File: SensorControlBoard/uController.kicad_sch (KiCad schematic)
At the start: 37 parts, among them J10 Conn_01x05_Pin, J11 USB_C_Receptacle_USB2.0, J2 Conn_01x02_Pin, J3 Conn_01x10_Pin, J4 Conn_01x10_Pin, J5 Conn_01x10_Pin, J6 Conn_01x02_Pin, J7 Conn_01x02_Pin, J8 Conn_01x02_Pin, SW1 SW_SPDT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

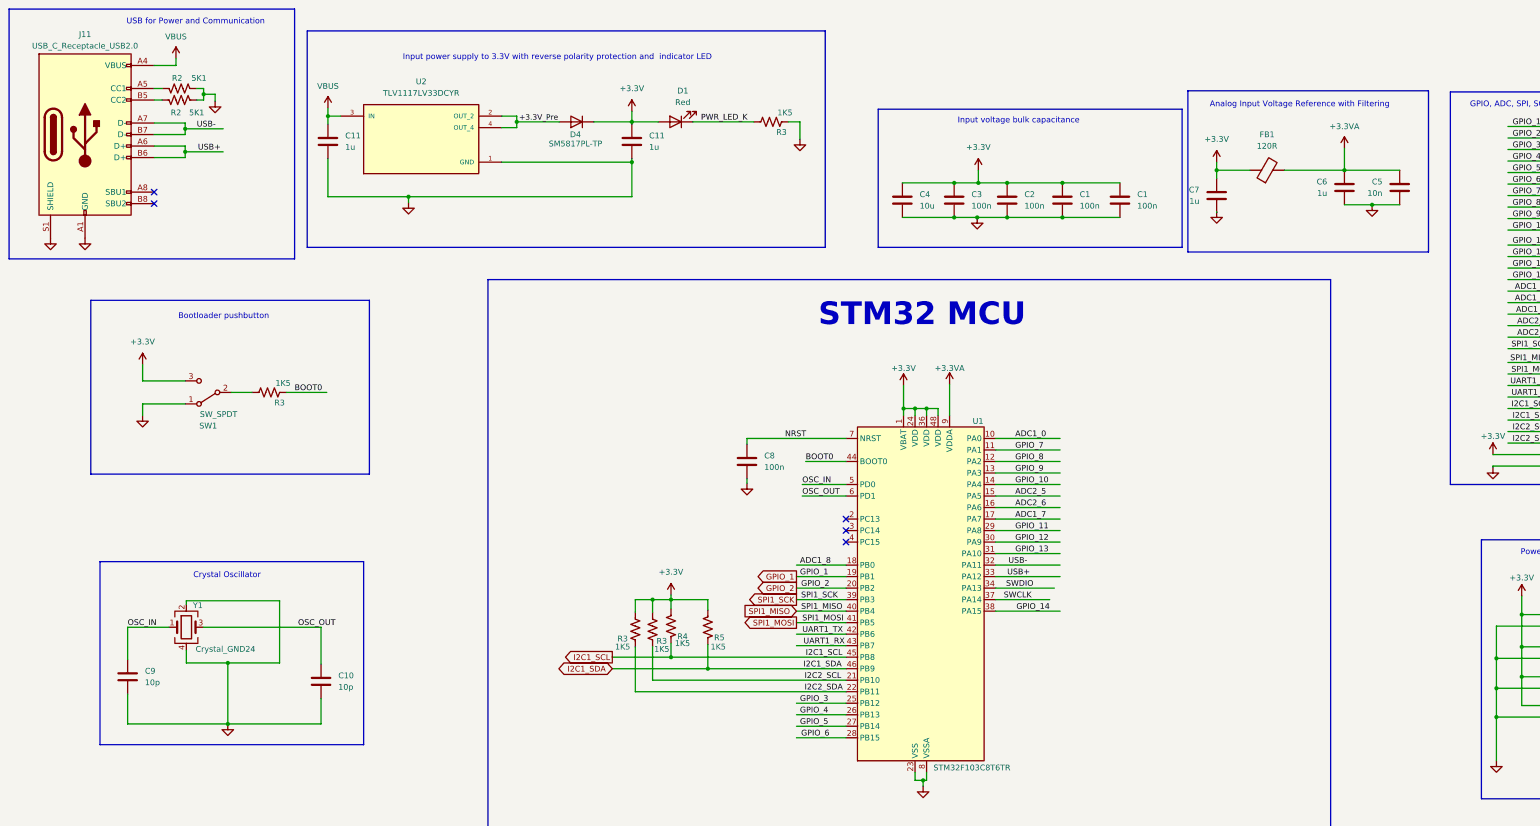
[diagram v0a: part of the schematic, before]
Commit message: Implemented ICM-42670-P 6 axis gyroscope/accelerometer
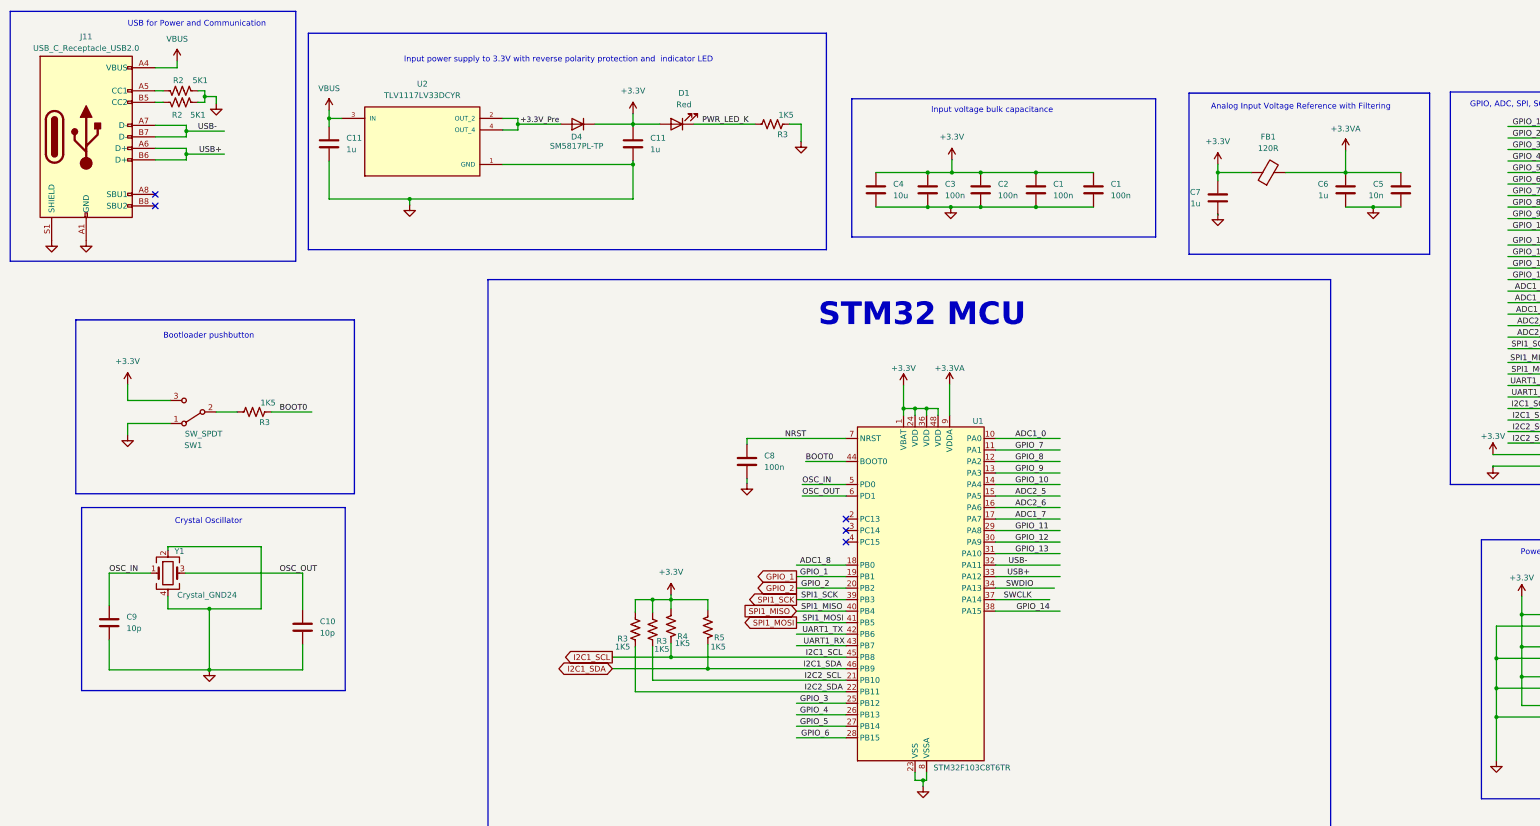
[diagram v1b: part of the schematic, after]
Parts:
- C1, C10, C11, C2, C3, C4, C5, C6, C7, C8, C9, D1, FB1, R2, R3, R4, R5, SW1, Y1: footprint (none) -> Resistor_SMD:R_0805_2012Metric
- J10: footprint (none) -> Connector_PinHeader_1.00mm:PinHeader_1x05_P1.00mm_Vertical
- J3: footprint (none) -> Connector_PinHeader_1.00mm:PinHeader_1x10_P1.00mm_Vertical
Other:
- moved on the sheet: C1, C10, C11, C2, C3, C4, C5, C6, C7, C9, D1, D4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

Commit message: Added more schematic documentation to prepare for hardware layout
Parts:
- Y1: value Crystal_GND24 -> 16MHz OSC; PN (none) -> X322516MMB4SI
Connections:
- net +3.3V: no longer J5.9 (Pin_9)
- net BOOT0: now also J5.10 (Pin_10)
- net GND: no longer J5.10 (Pin_10)
- net NRST: now also J5.9 (Pin_9)
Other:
- note added: "1: CS for TMAG5170 2: ALERT Pin for TMAG5170 3: ENABLE for LP5018 4: INT Pin for TMAG5273 5: CS for Micro-sd card 6: INT pin for OPT3002DNPR 7: INT1 for ICM-42670-P accel/gyro 8: INT2 for ICM-42670-P accel/gyro"
- note added: "1: SCL/SDA for TMAG5273 1: SCL/SDA for AT24CS04-XHM 1: SCL/SDA for ICM-42670-P accel/gyro 1: SCL/SDA for OPT3002DNPR 1: SCL/SDA for LP5018"
- note added: "1: for micro-sd card 1: for 5170"
- note added: "GPIO Used:"
- note added: "I2C Used:"
- note added: "SPI Used:"
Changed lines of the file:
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@@
   (junction (at 62.484 38.354) (diameter 0) (color 0 0 0 0)
   )
+  (junction (at 227.33 53.086) (diameter 0) (color 0 0 0 0)
+  )
   (junction (at 63.5 164.846) (diameter 0) (color 0 0 0 0)
   )
@@
   )
   (junction (at 221.996 62.738) (diameter 0) (color 0 0 0 0)
+  )
+  (junction (at 314.198 51.308) (diameter 0) (color 0 0 0 0)
   )
   (junction (at 245.872 55.118) (diameter 0) (color 0 0 0 0)
@@
     (stroke (width 0) (type default))
   )
-  (wire (pts (xy 314.198 50.292) (xy 314.198 55.118))
+  (wire (pts (xy 314.198 50.292) (xy 314.198 51.308))
     (stroke (width 0) (type default))
   )
@@
     (stroke (width 0) (type default))
   )
+  (wire (pts (xy 314.198 51.308) (xy 314.198 55.118))
+    (stroke (width 0) (type default))
+  )
   (wire (pts (xy 41.402 164.846) (xy 63.5 164.846))
     (stroke (width 0) (type default))
@@
     (stroke (width 0) (type default))
   )
-  (wire (pts (xy 346.71 119.888) (xy 359.41 119.888))
+  (wire (pts (xy 350.012 119.888) (xy 359.41 119.888))
     (stroke (width 0) (type default))
   )
@@
     (stroke (width 0) (type default))
   )
-  (wire (pts (xy 346.71 119.888) (xy 346.71 120.142))
-    (stroke (width 0) (type default))
-  )
   (wire (pts (xy 251.206 116.332) (xy 236.982 116.332))
     (stroke (width 0) (type default))
@@
     (stroke (width 0) (type default))
   )
+  (wire (pts (xy 227.33 53.086) (xy 227.33 55.118))
+    (stroke (width 0) (type default))
+  )
   (wire (pts (xy 350.012 104.648) (xy 359.41 104.648))
     (stroke (width 0) (type default))
@@
     (stroke (width 0) (type default))
   )
-  (wire (pts (xy 346.71 117.348) (xy 359.41 117.348))
+  (wire (pts (xy 350.012 117.348) (xy 359.41 117.348))
     (stroke (width 0) (type default))
   )
@@
     (stroke (width 0) (type default))
   )
-  (wire (pts (xy 227.33 52.324) (xy 227.33 55.118))
+  (wire (pts (xy 227.33 52.324) (xy 227.33 53.086))
     (stroke (width 0) (type default))
   )
@@
     (effects (font (size 1.27 1.27)) (justify left bottom))
   )
+  (text "I2C Used:\n" (at 32.004 214.376 0)
+    (effects (font (size 3 3) (thickness 0.6) bold) (justify left bottom))
+  )
   (text "Bootloader pushbutton\n" (at 53.34 91.948 0)
     (effects (font (size 1.27 1.27)) (justify left bottom))
+  )
+  (text "GPIO Used:" (at 32.004 239.014 0)
+    (effects (font (size 3 3) (thickness 0.6) bold) (justify left bottom))
+  )
+  (text "1: SCL/SDA for TMAG5273\n1: SCL/SDA for AT24CS04-XHM\n1: SCL/SDA for ICM-42670-P accel/gyro\n1: SCL/SDA for OPT3002DNPR\n1: SCL/SDA for LP5018\n\n\n\n"
+    (at 32.004 241.046 0)
+    (effects (font (size 2 2)) (justify left bottom))
   )
   (text "Analog Input Voltage Reference with Filtering\n" (at 284.48 41.402 0)
@@
     (effects (font (size 5 5) (thickness 1) bold) (justify left bottom))
   )
+  (text "SPI Used:\n" (at 32.766 200.66 0)
+    (effects (font (size 3 3) (thickness 0.6) bold) (justify left bottom))
+  )
   (text "Power and GND Breakouts\n" (at 352.806 139.7 0)
     (effects (font (size 1.27 1.27)) (justify left bottom))
@@
     (effects (font (size 1.27 1.27)) (justify left bottom))
   )
-  (text "USB for Power and Communication\n" (at 45.466 23.114 0)
-    (effects (font (size 1.27 1.27)) (justify left bottom))
+  (text "USB for Power and Communication\n" (at 33.02 22.606 0)
+    (effects (font (size 1.27 1.27)) (justify left bottom))
+  )
+  (text "1: CS for TMAG5170\n2: ALERT Pin for TMAG5170\n3: ENABLE for LP5018 \n4: INT Pin for TMAG5273\n5: CS for Micro-sd card\n6: INT pin for OPT3002DNPR\n7: INT1 for ICM-42670-P accel/gyro\n8: INT2 for ICM-42670-P accel/gyro\n\n\n"
+    (at 32.512 271.78 0)
+    (effects (font (size 2 2)) (justify left bottom))
+  )
+  (text "1: for micro-sd card\n1: for 5170\n\n" (at 33.02 210.312 0)
+    (effects (font (size 2 2)) (justify left bottom))
   )
   (text "Input voltage bulk capacitance\n" (at 222.758 42.164 0)
@@
     (effects (font (size 1.27 1.27)) (justify left bottom))
   )
+  (label "BOOT0" (at 351.282 119.888 0) (fields_autoplaced)
+    (effects (font (size 1.27 1.27)) (justify left bottom))
+  )
   (label "SWCLK" (at 238.76 149.352 0) (fields_autoplaced)
     (effects (font (size 1.27 1.27)) (justify left bottom))
@@
   )
   (label "NRST" (at 190.5 113.792 0) (fields_autoplaced)
+    (effects (font (size 1.27 1.27)) (justify left bottom))
+  )
+  (label "NRST" (at 351.282 117.348 0) (fields_autoplaced)
     (effects (font (size 1.27 1.27)) (justify left bottom))
   )
@@
     (property "Intersheetrefs" "${INTERSHEET_REFS}" (at 181.0439 149.352 0)
       (effects (font (size 1.27 1.27)) (justify right) hide)
-    )
-  )
-  (symbol (lib_id "power:+3.3V") (at 346.71 117.348 0) (unit 1)
-    (in_bom yes) (on_board yes) (dnp no)
-    (property "Reference" "#PWR016" (at 346.71 121.158 0)
-      (effects (font (size 1.27 1.27)) hide)
-    )
-    (property "Value" "+3.3V" (at 346.71 113.284 0)
-      (effects (font (size 1.27 1.27)))
-    )
-    (property "Footprint" "" (at 346.71 117.348 0)
-      (effects (font (size 1.27 1.27)) hide)
-    )
-    (property "Datasheet" "" (at 346.71 117.348 0)
-      (effects (font (size 1.27 1.27)) hide)
-    )
-    (pin "1")
-    (instances
-      (project "SensorControlBoard"
-        (path "/8c0c4014-aa51-4bf6-8434-aa4d122163d4"
-          (reference "#PWR016") (unit 1)
-        )
-        (path "/8c0c4014-aa51-4bf6-8434-aa4d122163d4/1219a1e8-5b4c-4ffc-965f-b8113c415640"
-          (reference "#PWR051") (unit 1)
-        )
-      )
     )
   )
@@
         (path "/8c0c4014-aa51-4bf6-8434-aa4d122163d4/1219a1e8-5b4c-4ffc-965f-b8113c415640"
           (reference "C6") (unit 1)
+        )
+      )
+    )
+  )
+  (symbol (lib_id "power:PWR_FLAG") (at 227.33 53.086 270) (unit 1)
+    (in_bom yes) (on_board yes) (dnp no)
+    (property "Reference" "#FLG02" (at 229.235 53.086 0)
+      (effects (font (size 1.27 1.27)) hide)
+    )
+    (property "Value" "PWR_FLAG" (at 230.124 53.086 90)
+      (effects (font (size 1.27 1.27)) (justify left))
+    )
+    (property "Footprint" "" (at 227.33 53.086 0)
+      (effects (font (size 1.27 1.27)) hide)
+    )
+    (property "Datasheet" "~" (at 227.33 53.086 0)
+      (effects (font (size 1.27 1.27)) hide)
+    )
+    (pin "1")
+    (instances
+      (project "SensorControlBoard"
+        (path "/8c0c4014-aa51-4bf6-8434-aa4d122163d4/1219a1e8-5b4c-4ffc-965f-b8113c415640"
+          (reference "#FLG02") (unit 1)
         )
       )
@@
       (effects (font (size 1.27 1.27)))
     )
-    (property "Value" "Crystal_GND24" (at 62.992 148.336 0)
+    (property "Value" "16MHz OSC" (at 62.992 148.336 0)
       (effects (font (size 1.27 1.27)))
     )
@@
     )
     (property "Datasheet" "~" (at 54.356 143.51 0)
+      (effects (font (size 1.27 1.27)) hide)
+    )
+    (property "PN" "X322516MMB4SI" (at 54.356 143.51 0)
       (effects (font (size 1.27 1.27)) hide)
     )
@@
         (path "/8c0c4014-aa51-4bf6-8434-aa4d122163d4/1219a1e8-5b4c-4ffc-965f-b8113c415640"
           (reference "C4") (unit 1)
-        )
-      )
-    )
-  )
-  (symbol (lib_id "power:GND") (at 346.71 120.142 0) (unit 1)
-    (in_bom yes) (on_board yes) (dnp no) (fields_autoplaced)
-    (property "Reference" "#PWR015" (at 346.71 126.492 0)
-      (effects (font (size 1.27 1.27)) hide)
-    )
-    (property "Value" "GND" (at 346.71 125.476 0)
-      (effects (font (size 1.27 1.27)) hide)
-    )
-    (property "Footprint" "" (at 346.71 120.142 0)
-      (effects (font (size 1.27 1.27)) hide)
-    )
-    (property "Datasheet" "" (at 346.71 120.142 0)
-      (effects (font (size 1.27 1.27)) hide)
-    )
-    (pin "1")
-    (instances
-      (project "SensorControlBoard"
-        (path "/8c0c4014-aa51-4bf6-8434-aa4d122163d4"
-          (reference "#PWR015") (unit 1)
-        )
-        (path "/8c0c4014-aa51-4bf6-8434-aa4d122163d4/1219a1e8-5b4c-4ffc-965f-b8113c415640"
-          (reference "#PWR052") (unit 1)
         )
       )
@@
         )
       )
+    )
+  )
+  (symbol (lib_id "power:PWR_FLAG") (at 314.198 51.308 270) (unit 1)
+    (in_bom yes) (on_board yes) (dnp no)
+    (property "Reference" "#FLG01" (at 316.103 51.308 0)
+      (effects (font (size 1.27 1.27)) hide)
+    )
+    (property "Value" "PWR_FLAG" (at 316.992 51.308 90)
+      (effects (font (size 1.27 1.27)) (justify left))
+    )
+    (property "Footprint" "" (at 314.198 51.308 0)
+      (effects (font (size 1.27 1.27)) hide)
+    )
+    (property "Datasheet" "~" (at 314.198 51.308 0)
+      (effects (font (size 1.27 1.27)) hide)
+    )
+    (pin "1")
+    (instances
+      (project "SensorControlBoard"
+        (path "/8c0c4014-aa51-4bf6-8434-aa4d122163d4/1219a1e8-5b4c-4ffc-965f-b8113c415640"
+          (reference "#FLG01") (unit 1)
+        )
+      )

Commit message: Initial placement done
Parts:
- removed J3, J4: Conn_01x10_Pin, Connector_PinHeader_1.00mm:PinHeader_1x10_P1.00mm_Vertical, symbol Connector:Conn_01x10_Pin
- added J3: Conn_02x10_Odd_Even, Connector_PinHeader_1.00mm:PinHeader_2x10_P1.00mm_Vertical, symbol Connector_Generic:Conn_02x10_Odd_Even
- C1, C2, C3, C8: footprint Resistor_SMD:R_0805_2012Metric -> Capacitor_SMD:C_0603_1608Metric_Pad1.08x0.95mm_HandSolder; MP (none) -> C0805C104K5RAC7210
- C10, C9: footprint Resistor_SMD:R_0805_2012Metric -> Capacitor_SMD:C_0603_1608Metric_Pad1.08x0.95mm_HandSolder; MP (none) -> C0805C100F3HAC7800
- C11, C6, C7: footprint Resistor_SMD:R_0805_2012Metric -> Capacitor_SMD:C_0603_1608Metric_Pad1.08x0.95mm_HandSolder; MP (none) -> C0805C105Z4VAC7800
- C4: footprint Resistor_SMD:R_0805_2012Metric -> Capacitor_SMD:C_0603_1608Metric_Pad1.08x0.95mm_HandSolder; MP (none) -> C0805C106K8PAC7800
- C5: footprint Resistor_SMD:R_0805_2012Metric -> Capacitor_SMD:C_0603_1608Metric_Pad1.08x0.95mm_HandSolder; MP (none) -> C0805C103K1RAC7800
- D1: footprint Resistor_SMD:R_0805_2012Metric -> LED_SMD:LED_0603_1608Metric_Pad1.05x0.95mm_HandSolder; MP (none) -> 150060AS75003
- D4: MP (none) -> SM5817PL-TP
- FB1: footprint Resistor_SMD:R_0805_2012Metric -> Resistor_SMD:R_0603_1608Metric_Pad0.98x0.95mm_HandSolder; MP (none) -> 2508051217Y6
- J11: footprint Connector_USB:USB_C_Receptacle_HRO_TYPE-C-31-M-12 -> USBC:USB_C_Receptacle_HRO_TYPE-C-31-M-12
- R2, R3, R4, R5: footprint Resistor_SMD:R_0805_2012Metric -> Resistor_SMD:R_0603_1608Metric_Pad0.98x0.95mm_HandSolder
- SW1: footprint Resistor_SMD:R_0805_2012Metric -> Connector:FanPinHeader_1x03_P2.54mm_Vertical; MP (none) -> EG1218
- Y1: footprint Resistor_SMD:R_0805_2012Metric -> Crystal:Crystal_SMD_3225-4Pin_3.2x2.5mm_HandSoldering
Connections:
- net +3.3V: now also U2.2 (OUT_2), U2.4 (OUT_4); no longer D4.1 (K)
- net ADC1_0: now also J3.10 (Pin_10)
- net ADC1_7: now also J3.12 (Pin_12)
- net ADC1_8: now also J3.14 (Pin_14)
- net ADC2_5: now also J3.16 (Pin_16)
- net ADC2_6: now also J3.18 (Pin_18)
- net GPIO_1: now also J3.1 (Pin_1)
- net GPIO_10: now also J3.19 (Pin_19)
- net GPIO_11: now also J3.2 (Pin_2)
- net GPIO_12: now also J3.4 (Pin_4)
- net GPIO_13: now also J3.6 (Pin_6)
- net GPIO_14: now also J3.8 (Pin_8)
- net GPIO_2: now also J3.3 (Pin_3)
- net GPIO_3: now also J3.5 (Pin_5)
- net GPIO_4: now also J3.7 (Pin_7)
- net GPIO_5: now also J3.9 (Pin_9)
- net GPIO_6: now also J3.11 (Pin_11)
- net GPIO_7: now also J3.13 (Pin_13)
- net GPIO_8: now also J3.15 (Pin_15)
- net GPIO_9: now also J3.17 (Pin_17)
- net SPI1_SCK: now also J3.20 (Pin_20)
- net VBUS: now also D4.1 (K); no longer J11.A4 (VBUS), J11.A9 (VBUS), J11.B4 (VBUS), J11.B9 (VBUS)
- net BOOT0_PP: now reaches R3.2, SW1.2 (B)
- removed net +3.3V_Pre: D4.2 (A), U2.2 (OUT_2), U2.4 (OUT_4)
- new net VBUS_USB: D4.2 (A), J11.A4 (VBUS), J11.A9 (VBUS), J11.B4 (VBUS), J11.B9 (VBUS)
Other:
- note added: "1: SCL/SDA for TMAG5273 (0x44/0x45) 1: SCL/SDA for AT24CS04-XHM (0xA0/0xA1) 1: SCL/SDA for ICM-42670-P accel/gyro (0xD0/0xD1) 1: SCL/SDA for OPT3002DNPR (0x88/0x89) 1: SCL/SDA for LP5018 (0x28)"
- note added: "FB value at 100MHz"
- note removed: "1: SCL/SDA for TMAG5273 1: SCL/SDA for AT24CS04-XHM 1: SCL/SDA for ICM-42670-P accel/gyro 1: SCL/SDA for OPT3002DNPR 1: SCL/SDA for LP5018"
- moved on the sheet: J10, J2, J5, J6, J7, J8, R3

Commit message: Initial Routing finished
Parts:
- removed J3: Conn_02x10_Odd_Even, Connector_PinHeader_1.00mm:PinHeader_2x10_P1.00mm_Vertical, symbol Connector_Generic:Conn_02x10_Odd_Even
- added GPIO1, GPIO10, GPIO2, GPIO3, GPIO4, GPIO5: TestPoint, TestPoint:TestPoint_Pad_1.0x1.0mm, symbol Connector:TestPoint
- added J5: Conn_01x10_Pin, Connector_PinHeader_1.00mm:PinHeader_1x10_P1.00mm_Vertical, symbol Connector:Conn_01x10_Pin
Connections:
- net +3.3V: now also J5.2 (Pin_2), J5.4 (Pin_4)
- net ADC1_0: now also J5.10 (Pin_10)
- net ADC1_7: now also J5.7 (Pin_7)
- net ADC1_8: now also J5.8 (Pin_8)
- net ADC2_5: now also J5.9 (Pin_9)
- net ADC2_6: now also J5.6 (Pin_6)
- net BOOT0: now also J5.1 (Pin_1); no longer J5.10 (Pin_10)
- net GND: now also J5.3 (Pin_3), J5.5 (Pin_5)
- net GPIO_1: now also GPIO1.1
- net GPIO_10: now also GPIO10.1
- net GPIO_2: now also GPIO2.1
- net GPIO_3: now also GPIO3.1
- net GPIO_4: now also GPIO4.1
- net GPIO_5: now also GPIO5.1
- net NRST: no longer J5.9 (Pin_9)
- net SPI1_SCK: now also J5.3 (Pin_3)
- net UART1_RX: now also J5.10 (Pin_10); no longer J5.4 (Pin_4)
- net UART1_TX: now also J5.9 (Pin_9); no longer J5.3 (Pin_3)
- no-connect marks 5 -> 6
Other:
- note added: "5: CS for Micro-sd card 6: ALERT Pin for TMAG5170 7: INT Pin for TMAG5273 8: ENABLE for LP5018 11: CS for TMAG5170 12: INT pin for OPT3002DNPR 13: INT2 for ICM-42670-P accel/gyro 14: INT1 for ICM-42670-P accel/gyro"
- note removed: "1: CS for TMAG5170 2: ALERT Pin for TMAG5170 3: ENABLE for LP5018 4: INT Pin for TMAG5273 5: CS for Micro-sd card 6: INT pin for OPT3002DNPR 7: INT1 for ICM-42670-P accel/gyro 8: INT2 for ICM-42670-P accel/gyro"
